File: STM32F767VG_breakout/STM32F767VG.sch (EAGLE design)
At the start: 42 parts, among them IC1 STM32F767VGT6, IC2 L7805CV, IC3 LD117AS33TR, X4 8MHz, X5 32.768kHz

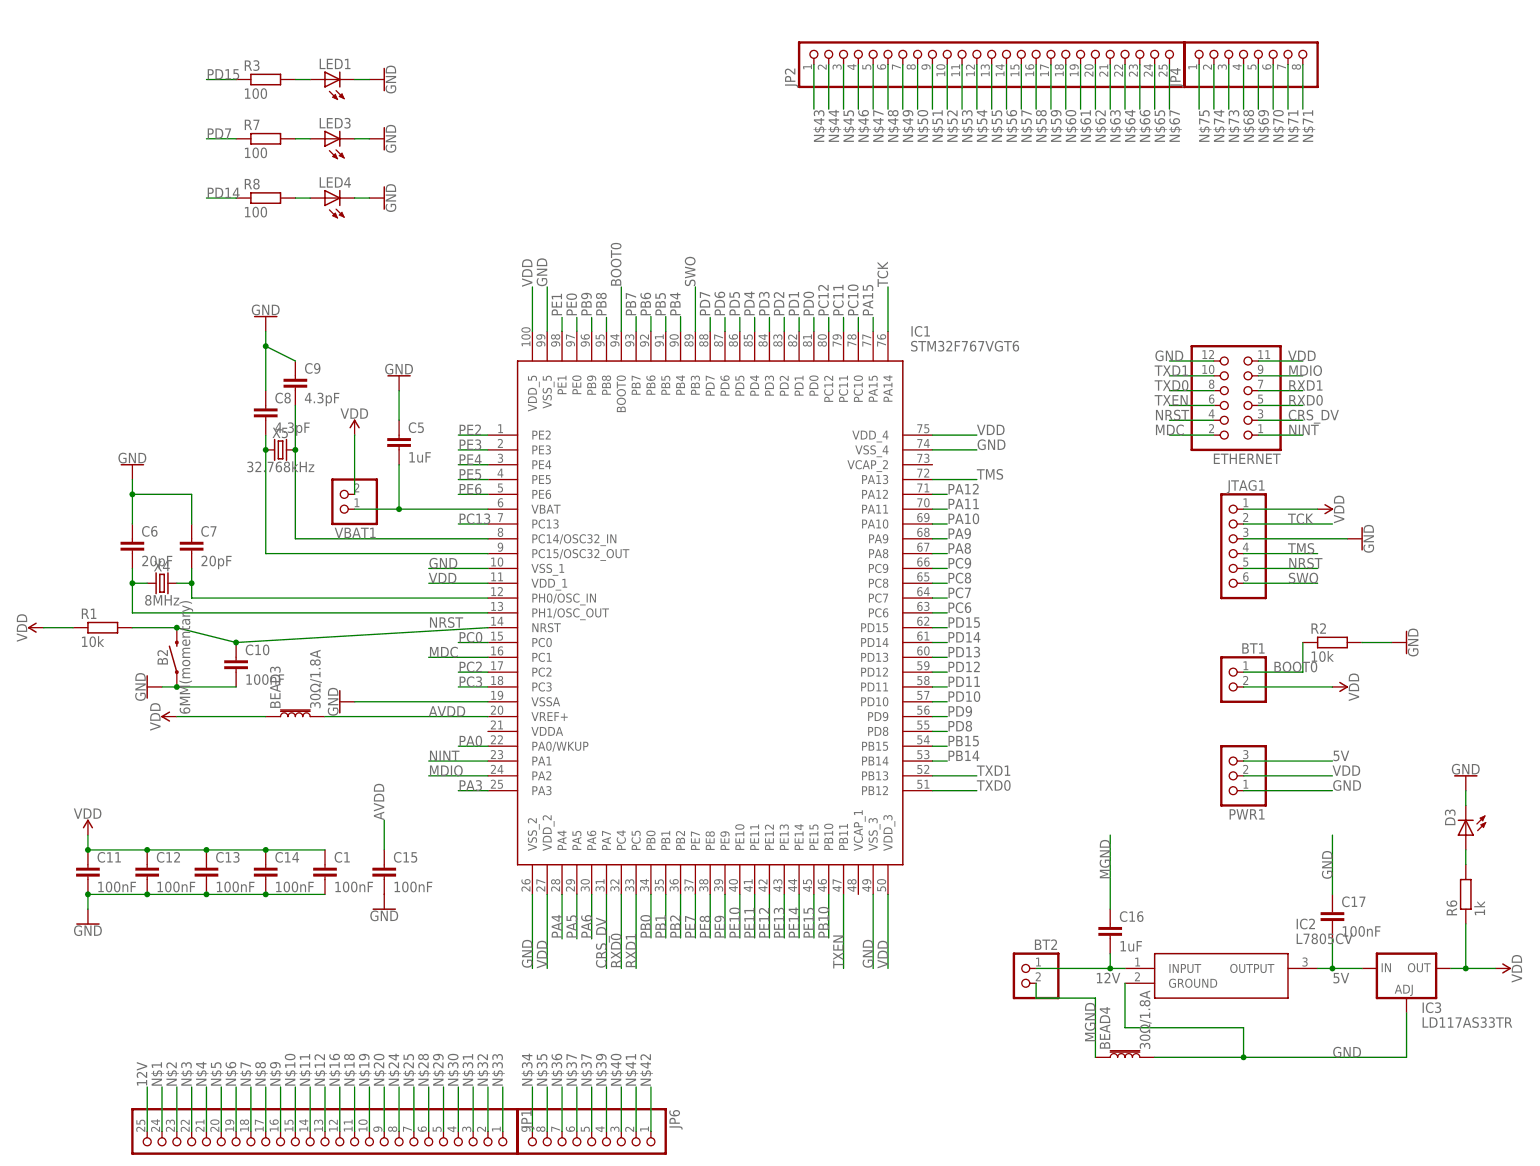
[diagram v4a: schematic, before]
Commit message: First try at routing everything
Currently it's a mess, so will redo most of the routing. But this is the current progress
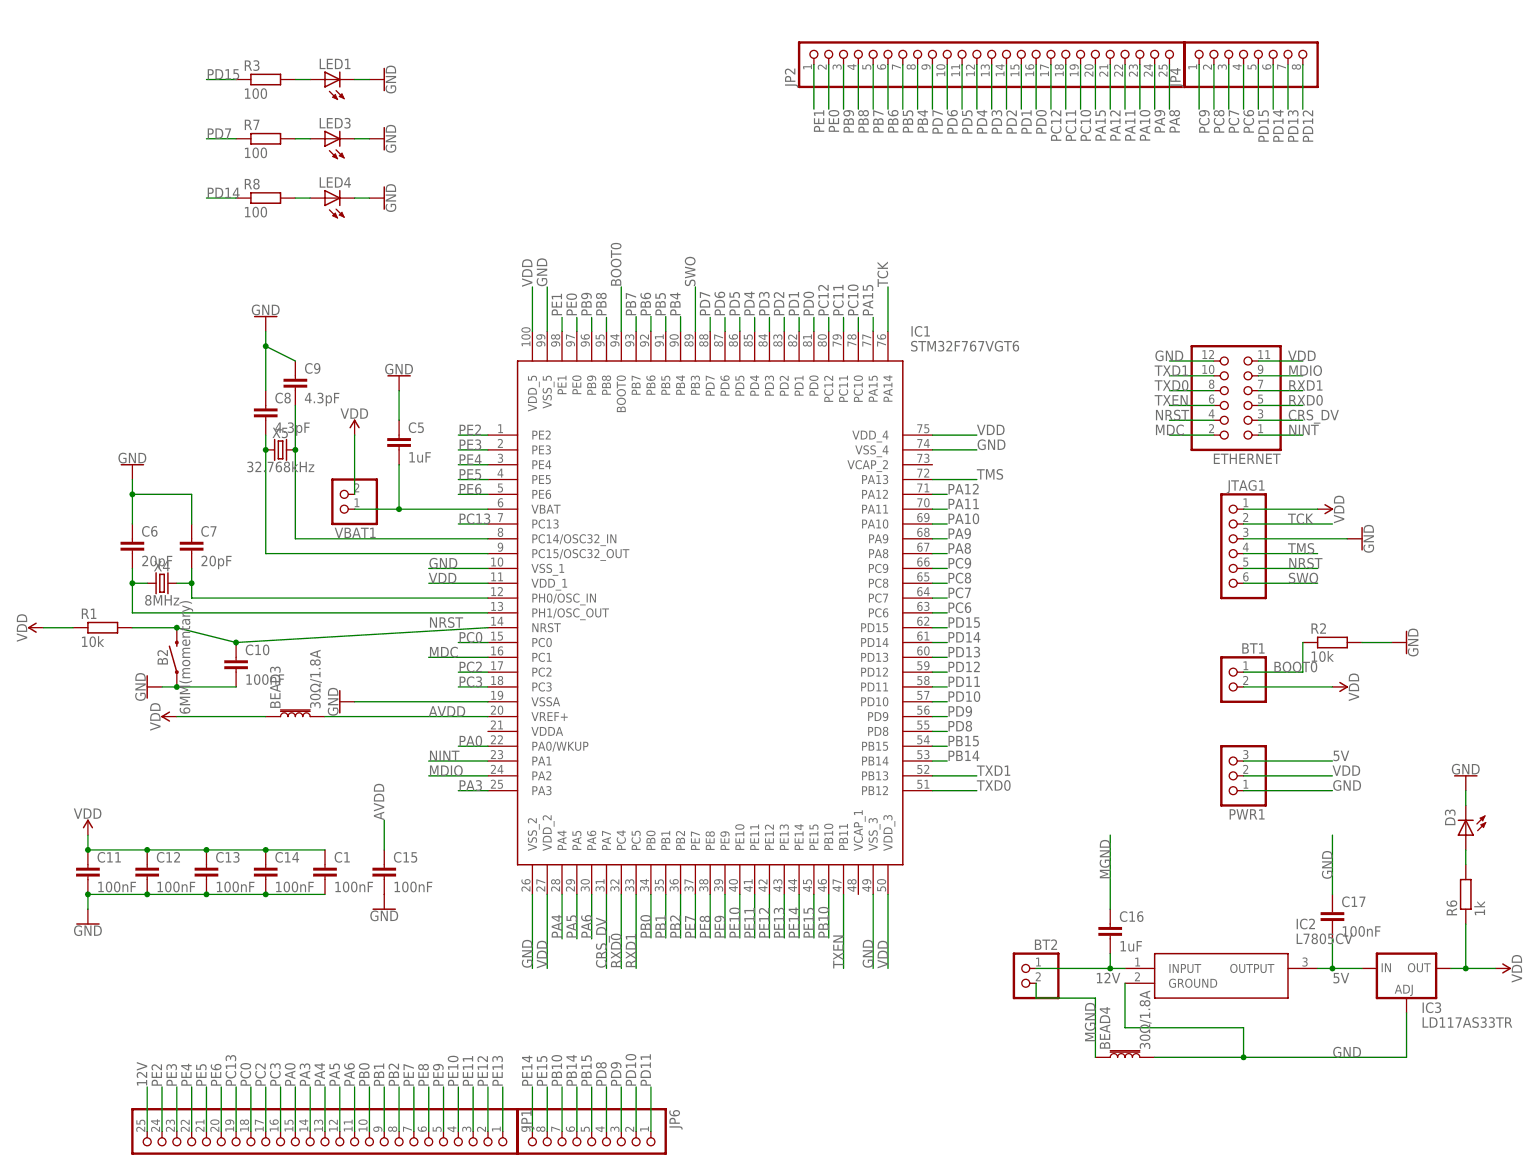
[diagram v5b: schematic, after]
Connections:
- removed net N$1: JP1.24
- removed net N$10: JP1.15
- removed net N$11: JP1.14
- removed net N$12: JP1.13
- removed net N$16: JP1.12
- removed net N$18: JP1.11
- removed net N$19: JP1.10
- removed net N$2: JP1.23
- removed net N$20: JP1.9
- removed net N$24: JP1.8
- removed net N$25: JP1.7
- removed net N$28: JP1.6
- removed net N$29: JP1.5
- removed net N$3: JP1.22
- removed net N$30: JP1.4
- removed net N$31: JP1.3
- removed net N$32: JP1.2
- removed net N$33: JP1.1
- removed net N$34: JP6.9
- removed net N$35: JP6.8
- removed net N$36: JP6.7
- removed net N$37: JP6.6
- removed net N$38: JP6.5
- removed net N$39: JP6.4
- removed net N$4: JP1.21
- removed net N$40: JP6.3
- removed net N$41: JP6.2
- removed net N$42: JP6.1
- removed net N$43: JP2.1
- removed net N$44: JP2.2
- removed net N$45: JP2.3
- removed net N$46: JP2.4
- removed net N$47: JP2.5
- removed net N$48: JP2.6
- removed net N$49: JP2.7
- removed net N$5: JP1.20
- removed net N$50: JP2.8
- removed net N$51: JP2.9
- removed net N$52: JP2.10
- removed net N$53: JP2.11
- removed net N$54: JP2.12
- removed net N$55: JP2.13
- removed net N$56: JP2.14
- removed net N$57: JP2.15
- removed net N$58: JP2.16
- removed net N$59: JP2.17
- removed net N$6: JP1.19
- removed net N$60: JP2.18
- removed net N$61: JP2.19
- removed net N$62: JP2.20
- removed net N$63: JP2.21
- removed net N$64: JP2.22
- removed net N$65: JP2.24
- removed net N$66: JP2.23
- removed net N$67: JP2.25
- removed net N$68: JP4.4
- removed net N$69: JP4.5
- removed net N$7: JP1.18
- removed net N$70: JP4.6
- removed net N$71: JP4.7
- removed net N$72: JP4.8
- removed net N$73: JP4.3
- removed net N$74: JP4.2
- removed net N$75: JP4.1
- removed net N$8: JP1.17
- removed net N$9: JP1.16
- net PA0: now also JP1.15
- net PA10: now also JP2.23
- net PA11: now also JP2.22
- net PA12: now also JP2.21
- net PA15: now also JP2.20
- net PA3: now also JP1.14
- net PA4: now also JP1.13
- net PA5: now also JP1.12
- net PA6: now also JP1.11
- net PA8: now also JP2.25
- net PA9: now also JP2.24
- net PB0: now also JP1.10
- net PB1: now also JP1.9
- net PB10: now also JP6.7
- net PB14: now also JP6.6
- net PB15: now also JP6.5
- net PB2: now also JP1.8
- net PB4: now also JP2.8
- net PB5: now also JP2.7
- net PB6: now also JP2.6
- net PB7: now also JP2.5
- net PB8: now also JP2.4
- net PB9: now also JP2.3
- net PC0: now also JP1.18
- net PC10: now also JP2.19
- net PC11: now also JP2.18
- net PC12: now also JP2.17
- net PC13: now also JP1.19
- net PC2: now also JP1.17
- net PC3: now also JP1.16
- net PC6: now also JP4.4
- net PC7: now also JP4.3
- net PC8: now also JP4.2
- net PC9: now also JP4.1
- net PD0: now also JP2.16
- net PD1: now also JP2.15
- net PD10: now also JP6.2
- net PD11: now also JP6.1
- net PD12: now also JP4.8
- net PD13: now also JP4.7
- net PD14: now also JP4.6
- net PD15: now also JP4.5
- net PD2: now also JP2.14
- net PD3: now also JP2.13
- net PD4: now also JP2.12
- net PD5: now also JP2.11
- net PD6: now also JP2.10
- net PD7: now also JP2.9
- net PD8: now also JP6.4
- net PD9: now also JP6.3
- net PE0: now also JP2.2
- net PE1: now also JP2.1
- net PE10: now also JP1.4
- net PE11: now also JP1.3
- net PE12: now also JP1.2
- net PE13: now also JP1.1
- net PE14: now also JP6.9
- net PE15: now also JP6.8
- net PE2: now also JP1.24
- net PE3: now also JP1.23
- net PE4: now also JP1.22
- net PE5: now also JP1.21
- net PE6: now also JP1.20
- net PE7: now also JP1.7
- net PE8: now also JP1.6
- net PE9: now also JP1.5
